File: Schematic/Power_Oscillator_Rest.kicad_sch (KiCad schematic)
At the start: 33 parts, among them J1 Barrel_Jack_Switch_Pin3Ring, SW1 SW_DPDT_x2, SW2 SW_Push, SW3 SW_Push, U1 L7805, U2 ATF16V8B, U4 74LS373, U6 M48Z35, U8 74LS374, Y1 Crystal (11.0592 MHz)

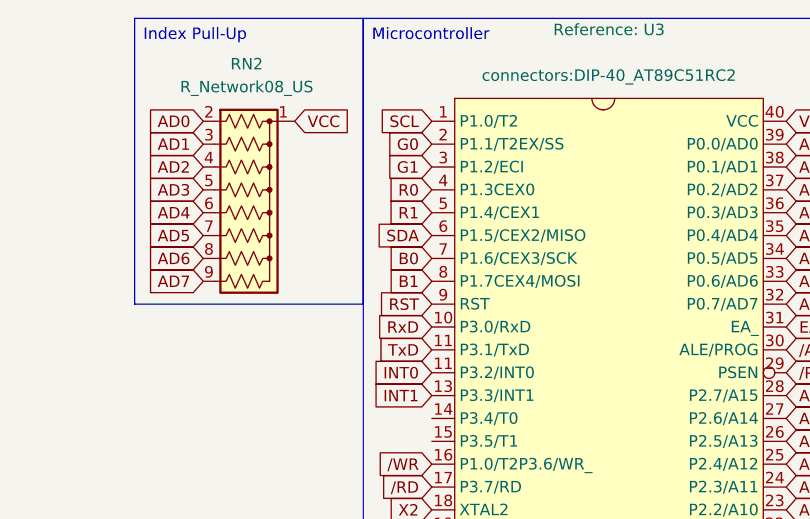
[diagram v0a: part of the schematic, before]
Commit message: fixed for different LCDs
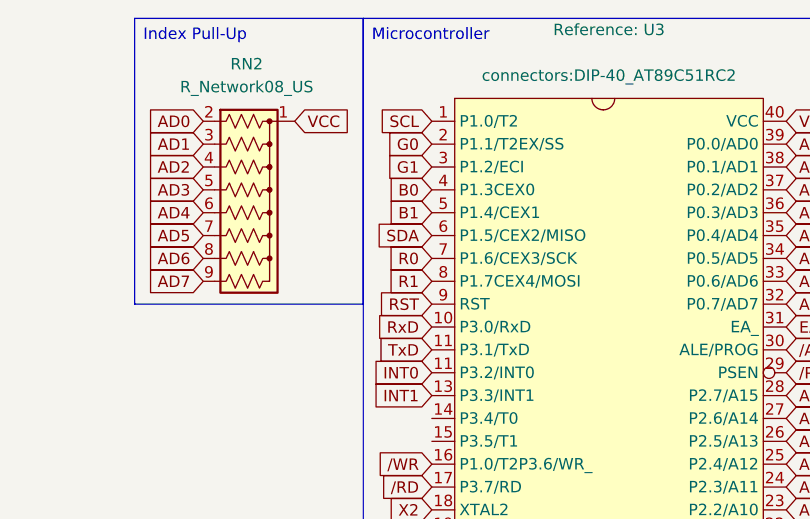
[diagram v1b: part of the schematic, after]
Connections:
- net B0: now also U3.4 (P1.3CEX0); no longer U3.7 (P1.6/CEX3/SCK)
- net B1: now also U3.5 (P1.4/CEX1); no longer U3.8 (P1.7CEX4/MOSI)
- net R0: now also U3.7 (P1.6/CEX3/SCK); no longer U3.4 (P1.3CEX0)
- net R1: now also U3.8 (P1.7CEX4/MOSI); no longer U3.5 (P1.4/CEX1)

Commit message: updated make and circuit
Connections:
- net R0 is gone; now on net SDA: U3.7 (P1.6/CEX3/SCK)
- net A15orWR: no longer U2.17 (I/O)
- net EA_: now also JP2.2 (B); no longer JP2.1 (A)
- net GND: no longer JP2.2 (B)
- net SCL: now also U3.6 (P1.5/CEX2/MISO); no longer U3.1 (P1.0/T2)
- net SDA: no longer U3.6 (P1.5/CEX2/MISO)
- net VCC: now also JP2.1 (A)
- net CS0: now reaches U3.14 (P3.4/T0)
- net CS1: now reaches U3.15 (P3.5/T1)
- net B0 renamed ADC5
- net B1 renamed ADC6
- net G0 renamed ADC3
- net G1 renamed ADC4
- net LCD_E: no longer names the net of U2.16 (I/O)
- net R1 renamed CMD
- new net ADC2: U3.1 (P1.0/T2)
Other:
- added sheet LCDs (untitled.kicad_sch)
- sheet VGA and ADC ports: added 8051 C0, 8051 C1, 8051 C2, 8051 C3, 8051 C4, 8051 C5; removed 8051 B0, 8051 B1, 8051 G0, 8051 G1, 8051 R0, 8051 R1
- moved on the sheet: JP2

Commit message: updated schematic
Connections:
- net A12: no longer U2.4 (PD/I3)
- net A13: no longer U2.5 (I4)
- net A14: no longer U2.6 (I5)
- net A15: now also U2.4 (PD/I3); no longer U2.7 (I6)
- net RST: now also U2.3 (I2)
- net /PSEN: now also U2.2 (I1); no longer U2.9 (I8)
- net /RD: now also U2.9 (I8); no longer U2.2 (I1)
- net !RST: now reaches U2.17 (I/O)
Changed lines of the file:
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@@
 	(wire
 		(pts
-			(xy 247.65 146.05) (xy 254 146.05)
-		)
-		(stroke
-			(width 0)
-			(type default)
-		)
-	)
-	(wire
-		(pts
 			(xy 99.06 78.74) (xy 104.14 78.74)
 		)
@@
 	(wire
 		(pts
+			(xy 245.11 143.51) (xy 254 143.51)
+		)
+		(stroke
+			(width 0)
+			(type default)
+		)
+	)
+	(wire
+		(pts
 			(xy 20.32 161.29) (xy 20.32 167.64)
 		)
@@
 	(wire
 		(pts
-			(xy 247.65 148.59) (xy 254 148.59)
-		)
-		(stroke
-			(width 0)
-			(type default)
-		)
-	)
-	(wire
-		(pts
 			(xy 247.65 151.13) (xy 254 151.13)
 		)
@@
 	(wire
 		(pts
-			(xy 245.11 143.51) (xy 254 143.51)
-		)
-		(stroke
-			(width 0)
-			(type default)
-		)
-	)
-	(wire
-		(pts
 			(xy 15.24 130.81) (xy 15.24 134.62)
 		)
@@
 		)
 	)
+	(global_label "A15"
+		(shape input)
+		(at 245.11 143.51 180)
+		(fields_autoplaced yes)
+		(effects
+			(font
+				(size 1.27 1.27)
+			)
+			(justify right)
+		)
+		(property "Intersheetrefs" "${INTERSHEET_REFS}"
+			(at 238.6172 143.51 0)
+			(effects
+				(font
+					(size 1.27 1.27)
+				)
+				(justify right)
+				(hide yes)
+			)
+		)
+	)
 	(global_label "AD11"
 		(shape input)
@@
 		)
 	)
-	(global_label "{slash}PSEN"
-		(shape input)
-		(at 247.65 156.21 180)
-		(fields_autoplaced yes)
-		(effects
-			(font
-				(size 1.27 1.27)
-			)
-			(justify right)
-		)
-		(property "Intersheetrefs" "${INTERSHEET_REFS}"
-			(at 238.3753 156.21 0)
-			(effects
-				(font
-					(size 1.27 1.27)
-				)
-				(justify right)
-				(hide yes)
-			)
-		)
-	)
 	(global_label "ADC5"
 		(shape input)
@@
 		)
 	)
-	(global_label "A15"
+	(global_label "AD5"
 		(shape input)
-		(at 247.65 151.13 180)
+		(at 55.88 161.29 90)
 		(fields_autoplaced yes)
 		(effects
@@
 				(size 1.27 1.27)
 			)
-			(justify right)
+			(justify left)
 		)
 		(property "Intersheetrefs" "${INTERSHEET_REFS}"
-			(at 241.1572 151.13 0)
+			(at 55.88 154.7367 90)
 			(effects
 				(font
 					(size 1.27 1.27)
 				)
-				(justify right)
+				(justify left)
 				(hide yes)
 			)
 		)
 	)
-	(global_label "AD5"
+	(global_label "AD4"
 		(shape input)
-		(at 55.88 161.29 90)
+		(at 273.05 36.83 0)
 		(fields_autoplaced yes)
 		(effects
@@
 		)
 		(property "Intersheetrefs" "${INTERSHEET_REFS}"
-			(at 55.88 154.7367 90)
+			(at 279.6033 36.83 0)
 			(effects
 				(font
@@
 		)
 	)
-	(global_label "AD4"
+	(global_label "!RST"
 		(shape input)
-		(at 273.05 36.83 0)
+		(at 24.13 161.29 90)
 		(fields_autoplaced yes)
 		(effects
@@
 		)
 		(property "Intersheetrefs" "${INTERSHEET_REFS}"
-			(at 279.6033 36.83 0)
+			(at 24.13 154.2529 90)
 			(effects
 				(font
@@
 		)
 	)
+	(global_label "RST"
+		(shape input)
+		(at 247.65 140.97 180)
+		(fields_autoplaced yes)
+		(effects
+			(font
+				(size 1.27 1.27)
+			)
+			(justify right)
+		)
+		(property "Intersheetrefs" "${INTERSHEET_REFS}"
+			(at 241.2177 140.97 0)
+			(effects
+				(font
+					(size 1.27 1.27)
+				)
+				(justify right)
+				(hide yes)
+			)
+		)
+	)
 	(global_label "AD1"
 		(shape input)
@@
 		)
 	)
-	(global_label "Q2"
+	(global_label "{slash}PSEN"
 		(shape input)
-		(at 252.73 106.68 180)
+		(at 247.65 138.43 180)
 		(fields_autoplaced yes)
 		(effects
@@
 		)
 		(property "Intersheetrefs" "${INTERSHEET_REFS}"
-			(at 247.2048 106.68 0)
+			(at 238.3753 138.43 0)
 			(effects
 				(font
@@
 		)
 	)
-	(global_label "{slash}RD"
+	(global_label "Q2"
 		(shape input)
-		(at 247.65 138.43 180)
+		(at 252.73 106.68 180)
 		(fields_autoplaced yes)
 		(effects
@@
 		)
 		(property "Intersheetrefs" "${INTERSHEET_REFS}"
-			(at 240.7943 138.43 0)
+			(at 247.2048 106.68 0)
 			(effects
 				(font
@@
 		)
 	)
-	(global_label "VCC"
+	(global_label "!RST"
 		(shape input)
-		(at 271.78 135.89 0)
+		(at 271.78 143.51 0)
 		(fields_autoplaced yes)
 		(effects
@@
 		)
 		(property "Intersheetrefs" "${INTERSHEET_REFS}"
-			(at 278.3938 135.89 0)
+			(at 278.8171 143.51 0)
 			(effects
 				(font
@@
 		)
 	)
-	(global_label "A13"
+	(global_label "VCC"
 		(shape input)
-		(at 247.65 146.05 180)
+		(at 271.78 135.89 0)
 		(fields_autoplaced yes)
 		(effects
@@
 				(size 1.27 1.27)
 			)
-			(justify right)
+			(justify left)
 		)
 		(property "Intersheetrefs" "${INTERSHEET_REFS}"
-			(at 241.1572 146.05 0)
+			(at 278.3938 135.89 0)
 			(effects
 				(font
 					(size 1.27 1.27)
 				)
-				(justify right)
+				(justify left)
 				(hide yes)
 			)
@@
 		)
 	)
-	(global_label "A12"
-		(shape input)
-		(at 245.11 143.51 180)
-		(fields_autoplaced yes)
-		(effects
-			(font
-				(size 1.27 1.27)
-			)
-			(justify right)
-		)
-		(property "Intersheetrefs" "${INTERSHEET_REFS}"
-			(at 238.6172 143.51 0)
-			(effects
-				(font
-					(size 1.27 1.27)
-				)
-				(justify right)
-				(hide yes)
-			)
-		)
-	)
 	(global_label "A15"
 		(shape input)
@@
 		)
 	)
-	(global_label "A14"
-		(shape input)
-		(at 247.65 148.59 180)
-		(fields_autoplaced yes)
-		(effects
-			(font
-				(size 1.27 1.27)
-			)
-			(justify right)
-		)
-		(property "Intersheetrefs" "${INTERSHEET_REFS}"
-			(at 241.1572 148.59 0)
-			(effects
-				(font
-					(size 1.27 1.27)
-				)
-				(justify right)
-				(hide yes)
-			)
-		)
-	)
 	(global_label "AD0"
 		(shape input)
@@
 		)
 	)
-	(global_label "RST"
+	(global_label "AD3"
 		(shape input)
-		(at 24.13 161.29 90)
+		(at 196.85 97.79 0)
 		(fields_autoplaced yes)
 		(effects
@@
 		)
 		(property "Intersheetrefs" "${INTERSHEET_REFS}"
-			(at 24.13 154.8577 90)
+			(at 203.4033 97.79 0)
 			(effects
 				(font
@@
 		)
 	)
-	(global_label "AD3"
+	(global_label "{slash}RD"
 		(shape input)
-		(at 196.85 97.79 0)
+		(at 247.65 156.21 180)
 		(fields_autoplaced yes)
 		(effects
@@
 				(size 1.27 1.27)
 			)
-			(justify left)
+			(justify right)
 		)
 		(property "Intersheetrefs" "${INTERSHEET_REFS}"
-			(at 203.4033 97.79 0)
+			(at 240.7943 156.21 0)
 			(effects
 				(font
 					(size 1.27 1.27)
 				)
-				(justify left)
+				(justify right)
 				(hide yes)
 			)
